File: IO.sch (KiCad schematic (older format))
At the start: 16 parts, among them U3 74AC541, U4 74LS138, U5 74HC245, U7 74LS148

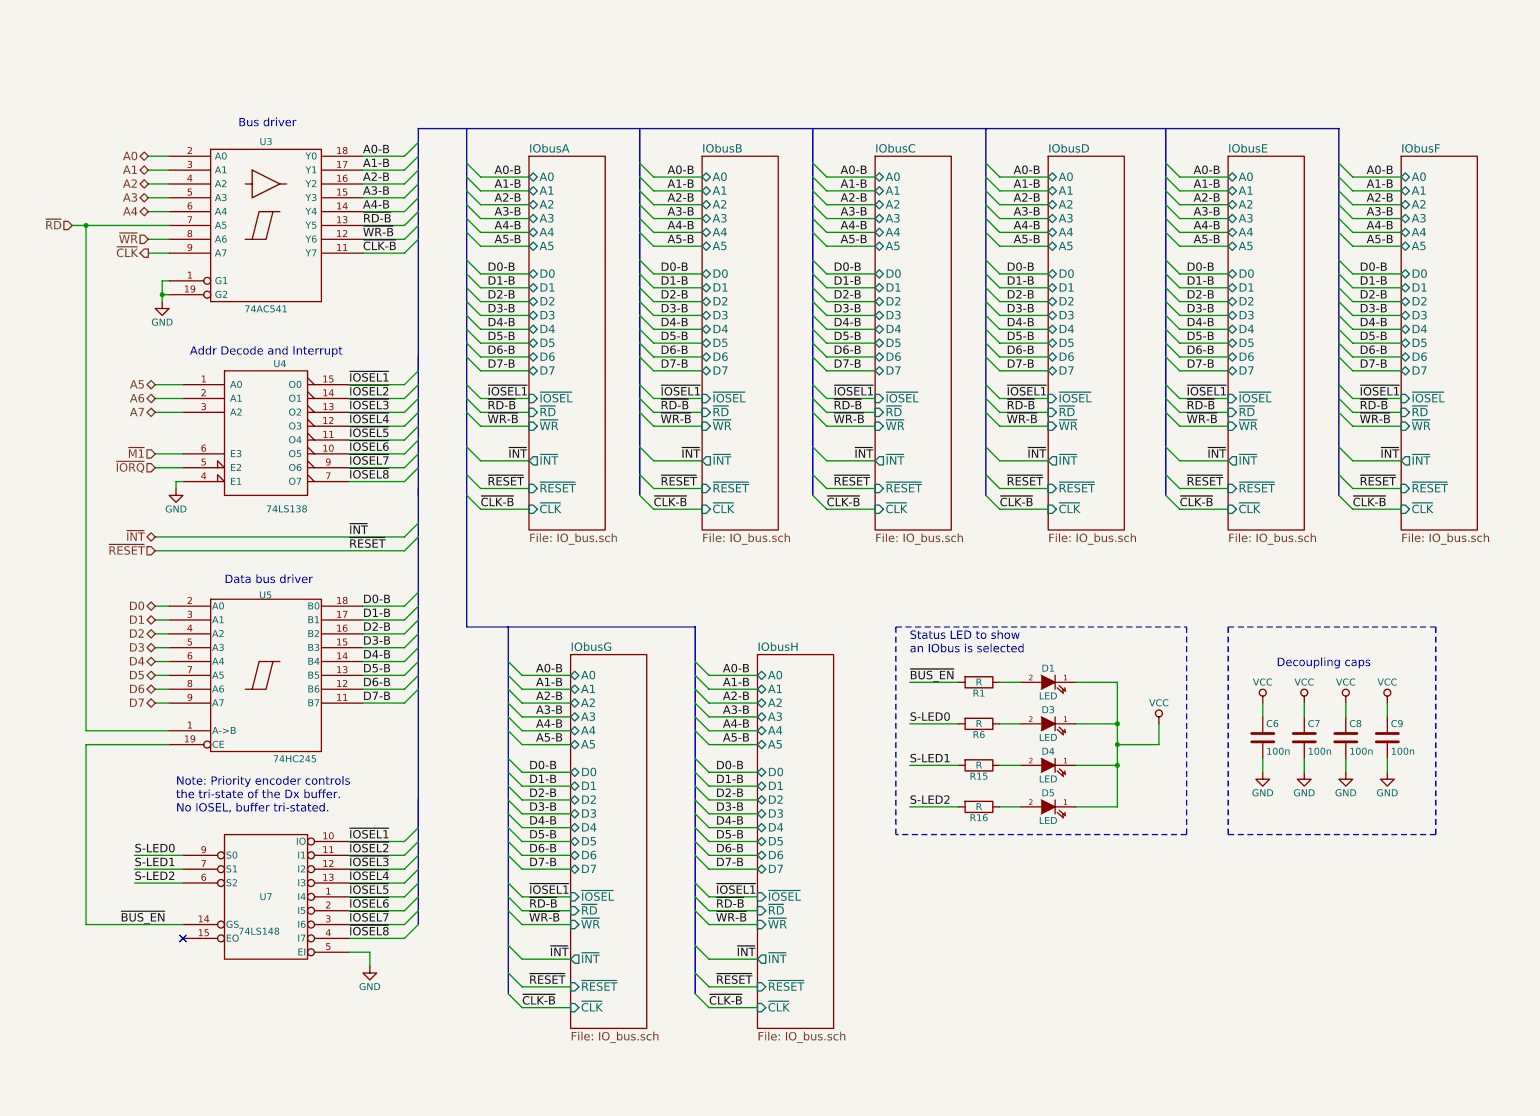
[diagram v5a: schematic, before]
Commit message: Added basic board layout WIP
Switched a few bus lines around to make the layout a little easier.
Still learning PCBNew, has a few quirks I haven't figured out yet.
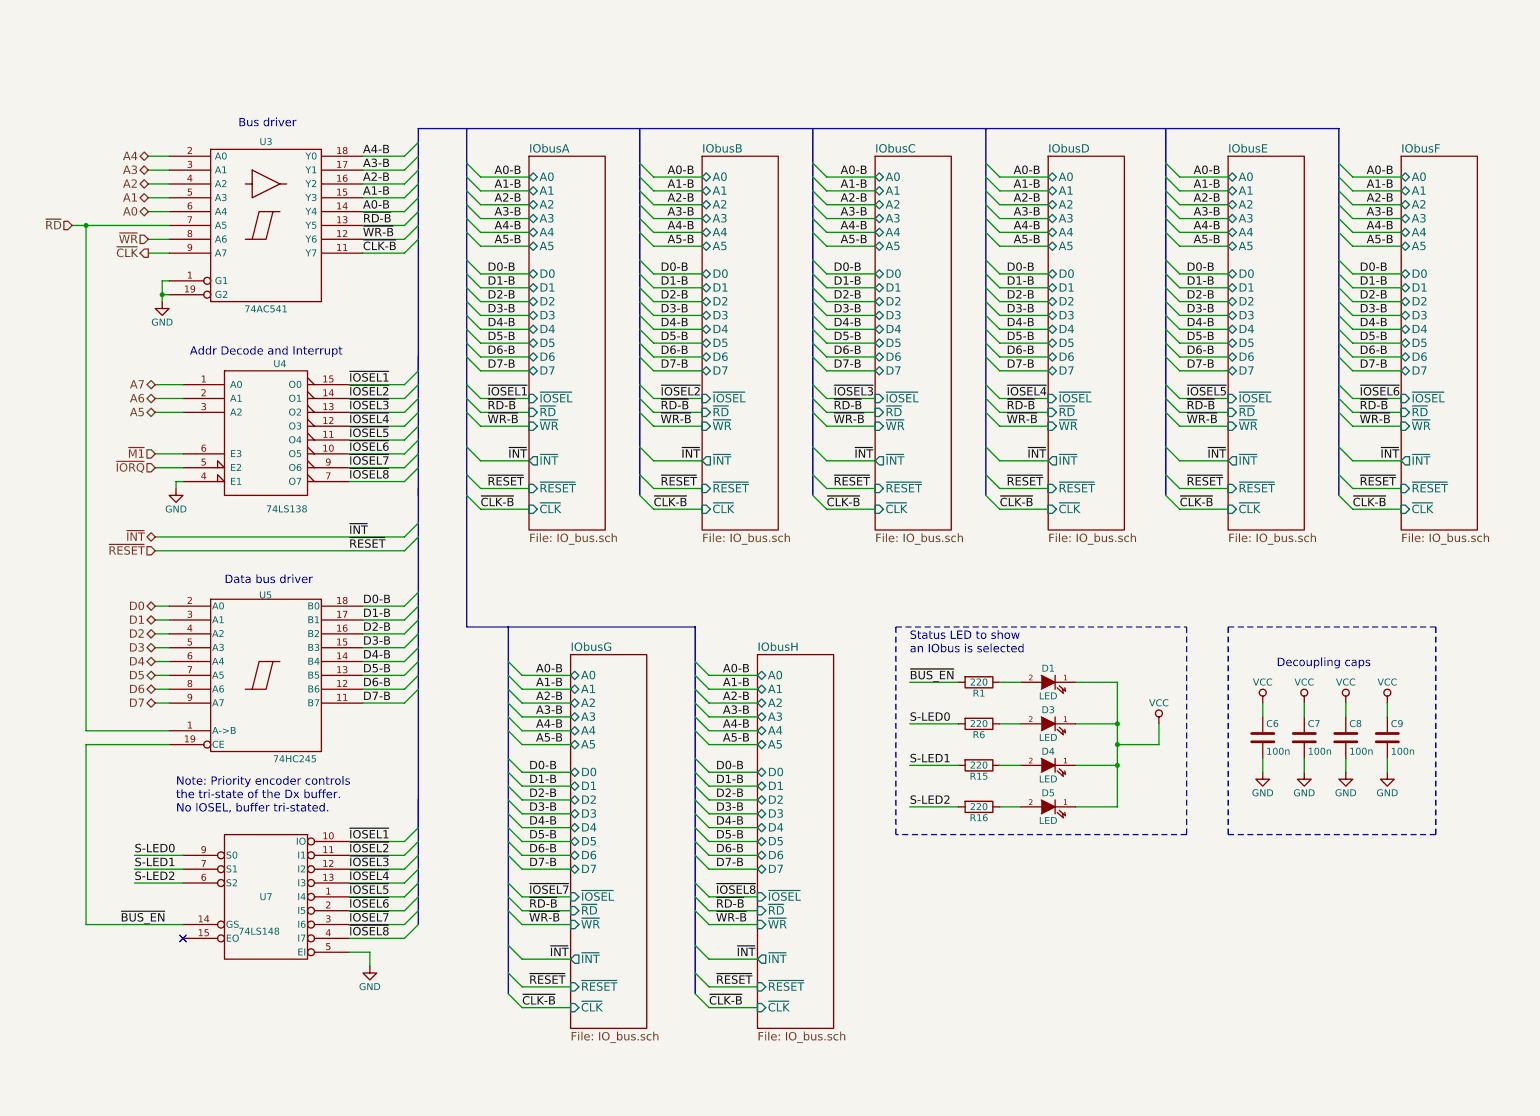
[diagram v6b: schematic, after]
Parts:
- D1, D3, D4, D5: footprint (none) -> LEDs:LED_1206
- R1, R15, R16, R6: value R -> 220; footprint (none) -> Resistors_SMD:R_0805_HandSoldering
- U7: footprint (none) -> Housings_DIP:DIP-16_W7.62mm_LongPads
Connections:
- net A0: now also U3.6 (A4); no longer U3.2 (A0)
- net A0-B: now also U3.14 (Y4); no longer U3.18 (Y0)
- net A1: now also U3.5 (A3); no longer U3.3 (A1)
- net A1-B: now also U3.15 (Y3); no longer U3.17 (Y1)
- net A3: now also U3.3 (A1); no longer U3.5 (A3)
- net A3-B: now also U3.17 (Y1); no longer U3.15 (Y3)
- net A4: now also U3.2 (A0); no longer U3.6 (A4)
- net A4-B: now also U3.18 (Y0); no longer U3.14 (Y4)
- net A5: now also U4.3 (A2); no longer U4.1 (A0)
- net A7: now also U4.1 (A0); no longer U4.3 (A2)
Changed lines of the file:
@@
 Comment4 ""
 $EndDescr
-Text HLabel 1400 950  0    60   3State ~ 0
+Text HLabel 1400 1350 0    60   3State ~ 0
 A0
-Text HLabel 1400 1050 0    60   3State ~ 0
+Text HLabel 1400 1250 0    60   3State ~ 0
 A1
 Text HLabel 1400 1150 0    60   3State ~ 0
 A2
-Text HLabel 1400 1250 0    60   3State ~ 0
+Text HLabel 1400 1050 0    60   3State ~ 0
 A3
-Text HLabel 1400 1350 0    60   3State ~ 0
+Text HLabel 1400 950  0    60   3State ~ 0
 A4
-Text HLabel 1450 2600 0    60   3State ~ 0
+Text HLabel 1450 2800 0    60   3State ~ 0
 A5
 Text HLabel 1450 2700 0    60   3State ~ 0
 A6
-Text HLabel 1450 2800 0    60   3State ~ 0
+Text HLabel 1450 2600 0    60   3State ~ 0
 A7
 Text HLabel 1450 4200 0    60   3State ~ 0
@@
 $EndSheet
 $Comp
-L GND #PWR015
+L GND #PWR018
 U 1 1 5780EA7D
 P 1500 2000
-F 0 "#PWR015" H 1500 1750 50  0001 C CNN
+F 0 "#PWR018" H 1500 1750 50  0001 C CNN
 F 1 "GND" H 1500 1850 50  0000 C CNN
 F 2 "" H 1500 2000 50  0000 C CNN
@@
 	3250 1550 3350 1450
 Text Label 2950 950  0    60   ~ 0
-A0-B
+A4-B
 Text Label 2950 1050 0    60   ~ 0
-A1-B
+A3-B
 Text Label 2950 1150 0    60   ~ 0
 A2-B
 Text Label 2950 1250 0    60   ~ 0
-A3-B
+A1-B
 Text Label 2950 1350 0    60   ~ 0
-A4-B
+A0-B
 Text Label 2950 1450 0    60   ~ 0
 ~RD-B
@@
 $EndComp
 $Comp
-L GND #PWR016
+L GND #PWR019
 U 1 1 57887A6E
 P 9450 5400
-F 0 "#PWR016" H 9450 5150 50  0001 C CNN
+F 0 "#PWR019" H 9450 5150 50  0001 C CNN
 F 1 "GND" H 9450 5250 50  0000 C CNN
 F 2 "" H 9450 5400 50  0000 C CNN
@@
 $EndComp
 $Comp
-L VCC #PWR017
+L VCC #PWR020
 U 1 1 57887A74
 P 9450 4900
-F 0 "#PWR017" H 9450 4750 50  0001 C CNN
+F 0 "#PWR020" H 9450 4750 50  0001 C CNN
 F 1 "VCC" H 9450 5050 50  0000 C CNN
 F 2 "" H 9450 4900 50  0000 C CNN
@@
 $EndComp
 $Comp
-L GND #PWR018
+L GND #PWR021
 U 1 1 57887A82
 P 9750 5400
-F 0 "#PWR018" H 9750 5150 50  0001 C CNN
+F 0 "#PWR021" H 9750 5150 50  0001 C CNN
 F 1 "GND" H 9750 5250 50  0000 C CNN
 F 2 "" H 9750 5400 50  0000 C CNN
@@
 $EndComp
 $Comp
-L VCC #PWR019
+L VCC #PWR022
 U 1 1 57887A88
 P 9750 4900
-F 0 "#PWR019" H 9750 4750 50  0001 C CNN
+F 0 "#PWR022" H 9750 4750 50  0001 C CNN
 F 1 "VCC" H 9750 5050 50  0000 C CNN
 F 2 "" H 9750 4900 50  0000 C CNN
@@
 $EndComp
 $Comp
-L GND #PWR020
+L GND #PWR023
 U 1 1 5785CC5B
 P 10050 5400
-F 0 "#PWR020" H 10050 5150 50  0001 C CNN
+F 0 "#PWR023" H 10050 5150 50  0001 C CNN
 F 1 "GND" H 10050 5250 50  0000 C CNN
 F 2 "" H 10050 5400 50  0000 C CNN
@@
 $EndComp
 $Comp
-L VCC #PWR021
+L VCC #PWR024
 U 1 1 5785CC61
 P 10050 4900
-F 0 "#PWR021" H 10050 4750 50  0001 C CNN
+F 0 "#PWR024" H 10050 4750 50  0001 C CNN
 F 1 "VCC" H 10050 5050 50  0000 C CNN
 F 2 "" H 10050 4900 50  0000 C CNN
@@
 $EndComp
 $Comp
-L GND #PWR022
+L GND #PWR025
 U 1 1 57897A09
 P 10350 5400
-F 0 "#PWR022" H 10350 5150 50  0001 C CNN
+F 0 "#PWR025" H 10350 5150 50  0001 C CNN
 F 1 "GND" H 10350 5250 50  0000 C CNN
 F 2 "" H 10350 5400 50  0000 C CNN
@@
 $EndComp
 $Comp
-L VCC #PWR023
+L VCC #PWR026
 U 1 1 57897A0F
 P 10350 4900
-F 0 "#PWR023" H 10350 4750 50  0001 C CNN
+F 0 "#PWR026" H 10350 4750 50  0001 C CNN
 F 1 "VCC" H 10350 5050 50  0000 C CNN
 F 2 "" H 10350 4900 50  0000 C CNN
@@
 F 0 "U7" H 2250 6300 50  0000 C CNN
 F 1 "74LS148" H 2300 6050 50  0000 C CNN
-F 2 "" H 2250 6300 50  0000 C CNN
+F 2 "Housings_DIP:DIP-16_W7.62mm_LongPads" H 2250 6300 50  0001 C CNN
 F 3 "" H 2250 6300 50  0000 C CNN
 	1    2250 6300
@@
 $EndComp
 $Comp
-L GND #PWR024
+L GND #PWR027
 U 1 1 5790EE64
 P 3000 6800
-F 0 "#PWR024" H 3000 6550 50  0001 C CNN
+F 0 "#PWR027" H 3000 6550 50  0001 C CNN
 F 1 "GND" H 3000 6650 50  0000 C CNN
 F 2 "" H 3000 6800 50  0000 C CNN
@@
 P 7400 4750
 F 0 "R1" V 7480 4750 50  0000 C CNN
-F 1 "R" V 7400 4750 50  0000 C CNN
-F 2 "" V 7330 4750 50  0000 C CNN
+F 1 "220" V 7400 4750 50  0000 C CNN
+F 2 "Resistors_SMD:R_0805_HandSoldering" H 7330 4750 50  0001 C CNN
 F 3 "" H 7400 4750 50  0000 C CNN
 	1    7400 4750
@@
 P 7400 5050
 F 0 "R6" V 7480 5050 50  0000 C CNN
-F 1 "R" V 7400 5050 50  0000 C CNN
-F 2 "" V 7330 5050 50  0000 C CNN
+F 1 "220" V 7400 5050 50  0000 C CNN
+F 2 "Resistors_SMD:R_0805_HandSoldering" H 7330 5050 50  0001 C CNN
 F 3 "" H 7400 5050 50  0000 C CNN
 	1    7400 5050
@@
 P 7400 5350
 F 0 "R15" V 7480 5350 50  0000 C CNN
-F 1 "R" V 7400 5350 50  0000 C CNN
-F 2 "" V 7330 5350 50  0000 C CNN
+F 1 "220" V 7400 5350 50  0000 C CNN
+F 2 "Resistors_SMD:R_0805_HandSoldering" H 7330 5350 50  0001 C CNN
 F 3 "" H 7400 5350 50  0000 C CNN
 	1    7400 5350
@@
 P 7400 5650
 F 0 "R16" V 7480 5650 50  0000 C CNN
-F 1 "R" V 7400 5650 50  0000 C CNN
-F 2 "" V 7330 5650 50  0000 C CNN
+F 1 "220" V 7400 5650 50  0000 C CNN
+F 2 "Resistors_SMD:R_0805_HandSoldering" H 7330 5650 50  0001 C CNN
 F 3 "" H 7400 5650 50  0000 C CNN
 	1    7400 5650
@@
 F 0 "D1" H 7900 4850 50  0000 C CNN
 F 1 "LED" H 7900 4650 50  0000 C CNN
-F 2 "" H 7900 4750 50  0000 C CNN
+F 2 "LEDs:LED_1206" H 7900 4750 50  0001 C CNN
 F 3 "" H 7900 4750 50  0000 C CNN
 	1    7900 4750
@@
 F 0 "D3" H 7900 5150 50  0000 C CNN
 F 1 "LED" H 7900 4950 50  0000 C CNN
-F 2 "" H 7900 5050 50  0000 C CNN
+F 2 "LEDs:LED_1206" H 7900 5050 50  0001 C CNN
 F 3 "" H 7900 5050 50  0000 C CNN
 	1    7900 5050
@@
 F 0 "D4" H 7900 5450 50  0000 C CNN
 F 1 "LED" H 7900 5250 50  0000 C CNN
-F 2 "" H 7900 5350 50  0000 C CNN
+F 2 "LEDs:LED_1206" H 7900 5350 50  0001 C CNN
 F 3 "" H 7900 5350 50  0000 C CNN
 	1    7900 5350
@@
 F 0 "D5" H 7900 5750 50  0000 C CNN
 F 1 "LED" H 7900 5550 50  0000 C CNN
-F 2 "" H 7900 5650 50  0000 C CNN
+F 2 "LEDs:LED_1206" H 7900 5650 50  0001 C CNN
 F 3 "" H 7900 5650 50  0000 C CNN
 	1    7900 5650
@@
 $EndComp
 $Comp
-L VCC #PWR025
+L VCC #PWR028
 U 1 1 5792ACFD
 P 8700 5050
-F 0 "#PWR025" H 8700 4900 50  0001 C CNN
+F 0 "#PWR028" H 8700 4900 50  0001 C CNN
 F 1 "VCC" H 8700 5200 50  0000 C CNN
 F 2 "" H 8700 5050 50  0000 C CNN
@@
 	1450 3200 1650 3200
 $Comp
-L GND #PWR026
+L GND #PWR029
 U 1 1 579690D1
 P 1600 3350
-F 0 "#PWR026" H 1600 3100 50  0001 C CNN
+F 0 "#PWR029" H 1600 3100 50  0001 C CNN
 F 1 "GND" H 1600 3200 50  0000 C CNN
 F 2 "" H 1600 3350 50  0000 C CNN
@@
 ~WR-B
 Text Label 4150 6300 0    60   ~ 0
-~IOSEL1
+~IOSEL7
 Text Label 4150 5400 0    60   ~ 0
 D0-B
@@
 ~WR-B
 Text Label 5500 6300 0    60   ~ 0
-~IOSEL1
+~IOSEL8
 Text Label 5500 5400 0    60   ~ 0
 D0-B
@@
 ~WR-B
 Text Label 5100 2700 0    60   ~ 0
-~IOSEL1
+~IOSEL2
 Text Label 5100 1800 0    60   ~ 0
 D0-B
@@
 ~WR-B
 Text Label 6350 2700 0    60   ~ 0
-~IOSEL1
+~IOSEL3
 Text Label 6350 1800 0    60   ~ 0
 D0-B
@@
 ~WR-B
 Text Label 7600 2700 0    60   ~ 0
-~IOSEL1
+~IOSEL4
 Text Label 7600 1800 0    60   ~ 0
 D0-B
@@
 ~WR-B
 Text Label 8900 2700 0    60   ~ 0
-~IOSEL1
+~IOSEL5
 Text Label 8900 1800 0    60   ~ 0
 D0-B
@@
 ~WR-B
 Text Label 10150 2700 0    60   ~ 0
-~IOSEL1
+~IOSEL6
 Text Label 10150 1800 0    60   ~ 0
 D0-B

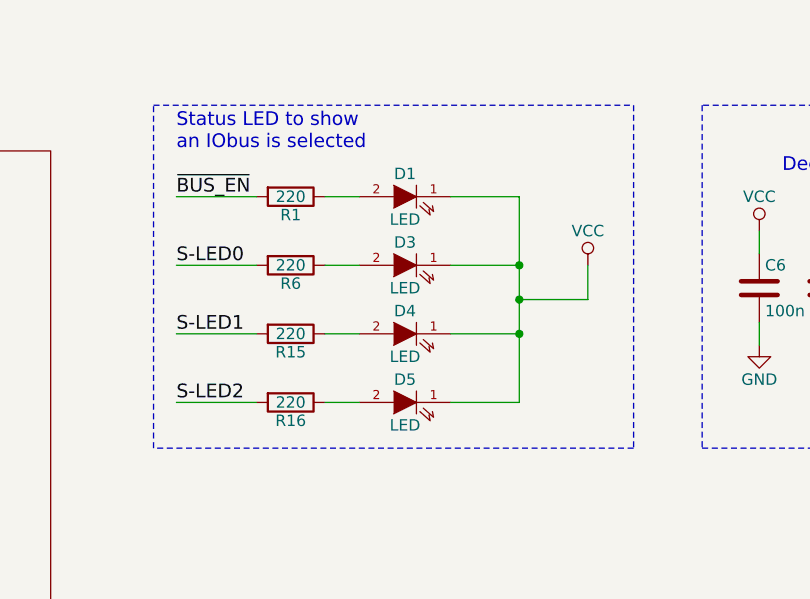
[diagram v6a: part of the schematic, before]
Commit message: Updated LEDs, added power supply options, added mounting holes in schematic.
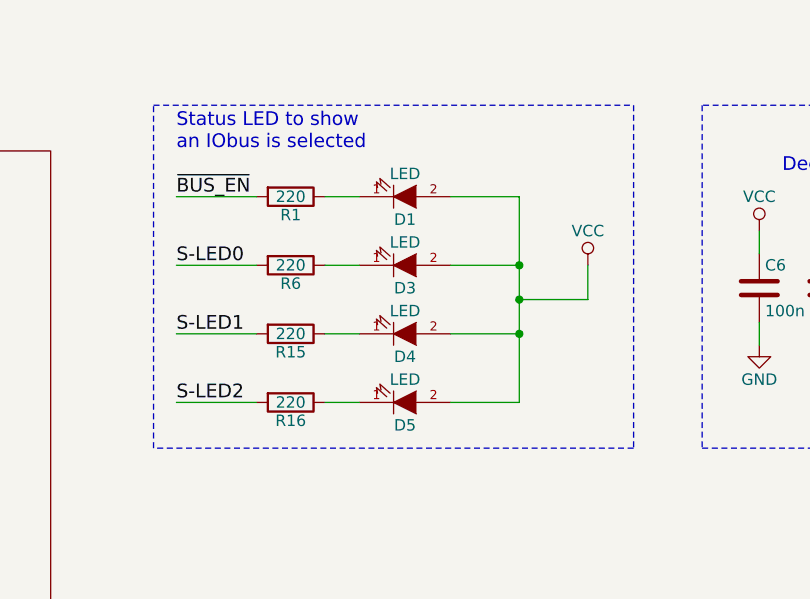
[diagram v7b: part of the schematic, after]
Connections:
- net VCC: now also D1.2 (A), D3.2 (A), D4.2 (A), D5.2 (A); no longer D1.1 (K), D3.1 (K), D4.1 (K), D5.1 (K)
- net at R1.1: now also D1.1 (K); no longer D1.2 (A)
- net at R6.1: now also D3.1 (K); no longer D3.2 (A)
- net at R15.1: now also D4.1 (K); no longer D4.2 (A)
- net at R16.1: now also D5.1 (K); no longer D5.2 (A)
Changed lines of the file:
@@
 LIBS:microchip_pic18mcu
 LIBS:6850
+LIBS:nrc2016
 LIBS:z80-cache
 EELAYER 25 0
@@
 F 3 "" H 7900 4750 50  0000 C CNN
 	1    7900 4750
-	-1   0    0    -1
+	1    0    0    1
 $EndComp
 $Comp
@@
 F 3 "" H 7900 5050 50  0000 C CNN
 	1    7900 5050
-	-1   0    0    -1
+	1    0    0    1
 $EndComp
 $Comp
@@
 F 3 "" H 7900 5350 50  0000 C CNN
 	1    7900 5350
-	-1   0    0    -1
+	1    0    0    1
 $EndComp
 $Comp
@@
 F 3 "" H 7900 5650 50  0000 C CNN
 	1    7900 5650
-	-1   0    0    -1
-$EndComp
-$Comp
+	1    0    0    1
+$EndComp
+$Comp
